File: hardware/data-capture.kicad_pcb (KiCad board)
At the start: 2 copper layers, 22 x 43.2 mm, 50 parts, among them J1 USB_B_Mini, J2 Conn_ARM_JTAG_SWD_10, J3 DM3AT-SF-PEJM5, J4 Conn_01x02, Q1 Q_PMOS_GSD, SW1 SW_Push, U1 MCP73831-2-OT, U2 TLV70218_SOT23-5, U3 AP2112K-3.3, U4 MDBT50Q-1M, U5 PCA9306, U6 ICM-20948, U7 BMP280, Y1 32.768

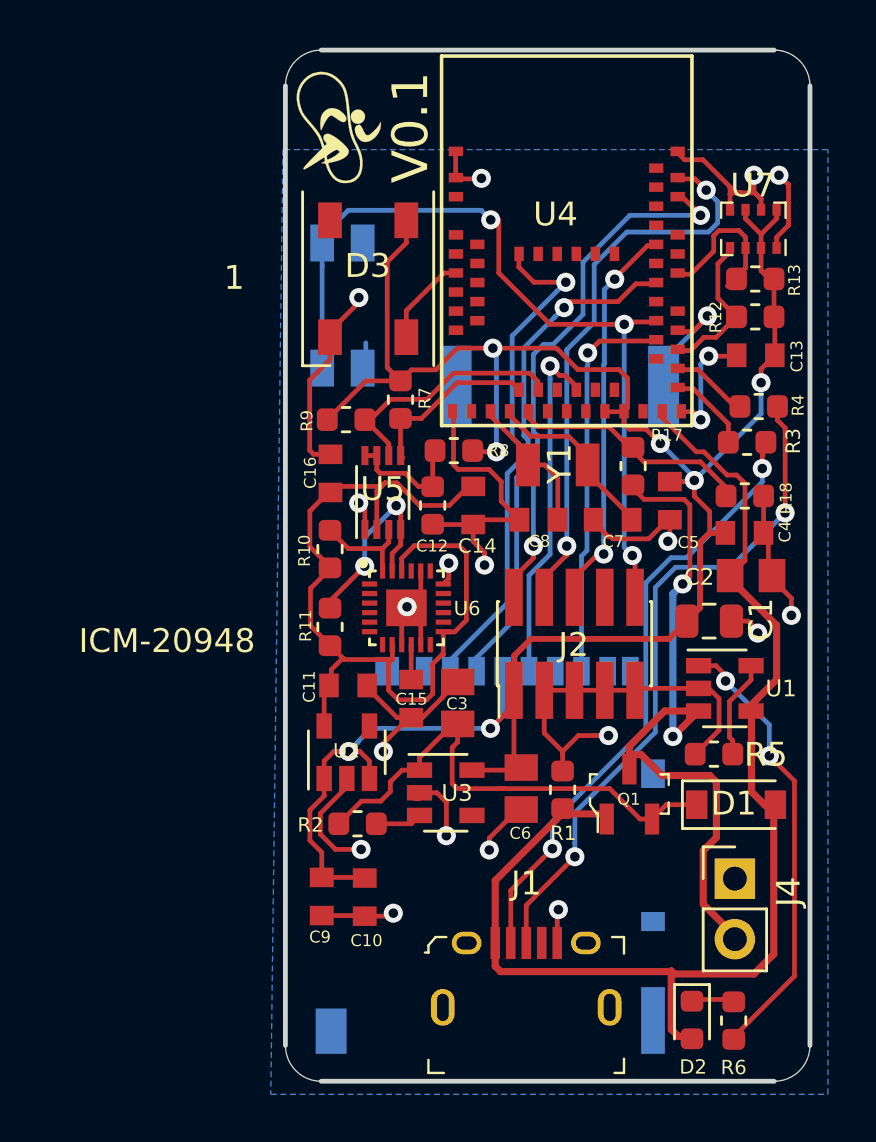
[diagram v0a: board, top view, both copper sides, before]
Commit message: update schematic for ESYNC for IMU
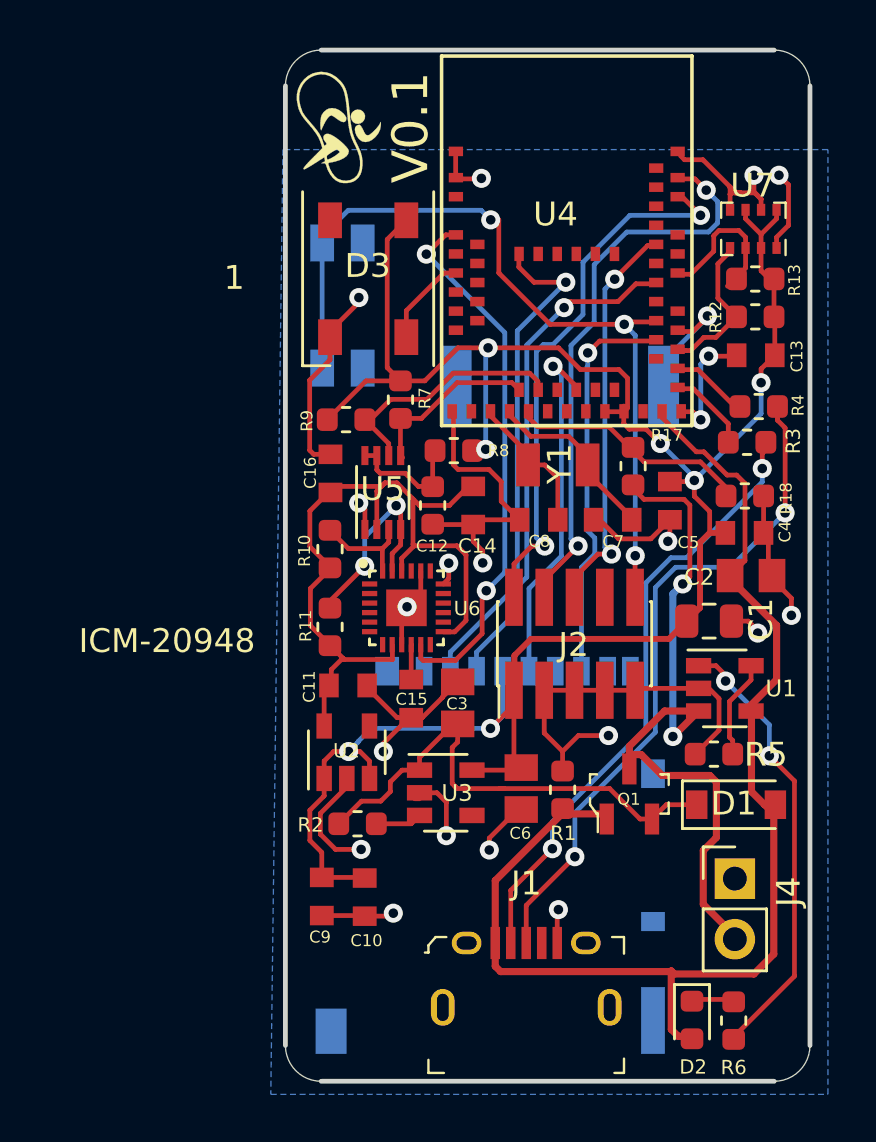
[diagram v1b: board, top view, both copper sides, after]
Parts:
- J2: value Conn_ARM_JTAG_SWD_10 -> Conn_ARM_JTAG_SWD_10-Connector_Specialized-bed-sensor-rescue-bed-sensor-rescue-bed-sensor-rescue-bed-sensor-rescue-bed-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
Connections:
- D3 pad 2: (no net) -> Net-(D3-Pad2)
- J1 pad 4: (no net) -> Net-(J1-Pad4)
- J2 pad 8: (no net) -> Net-(J2-Pad8)
- J3 pad 1: (no net) -> Net-(J3-Pad1)
- J3 pad 8: (no net) -> Net-(J3-Pad8)
- J3 pad SWA: (no net) -> Net-(J3-PadSWA)
- J3 pad SWB: (no net) -> Net-(J3-PadSWB)
- U2 pad 4: (no net) -> Net-(U2-Pad4)
- U3 pad 4: (no net) -> Net-(U3-Pad4)
- U4 pad 10: (no net) -> Net-(U4-Pad10)
- U4 pad 11: (no net) -> Net-(U4-Pad11)
- U4 pad 12: (no net) -> Net-(U4-Pad12)
- U4 pad 13: (no net) -> Net-(U4-Pad13)
- U4 pad 14: (no net) -> Net-(U4-Pad14)
- U4 pad 16: (no net) -> Net-(U4-Pad16)
- U4 pad 22: (no net) -> Net-(U4-Pad22)
- U4 pad 23: (no net) -> Net-(U4-Pad23)
- U4 pad 24: (no net) -> Net-(U4-Pad24)
- U4 pad 26: (no net) -> Net-(U4-Pad26)
- U4 pad 27: (no net) -> Net-(U4-Pad27)
- U4 pad 29: (no net) -> Net-(U4-Pad29)
- U4 pad 3: (no net) -> Net-(U4-Pad3)
- U4 pad 31: (no net) -> Net-(U4-Pad31)
- U4 pad 36: (no net) -> Net-(U4-Pad36)
- U4 pad 4: (no net) -> IMU_FSYC
- U4 pad 41: (no net) -> Net-(U4-Pad41)
- U4 pad 42: (no net) -> Net-(U4-Pad42)
- U4 pad 45: (no net) -> Net-(U4-Pad45)
- U4 pad 46: (no net) -> Net-(U4-Pad46)
- U4 pad 48: (no net) -> Net-(U4-Pad48)
- U4 pad 5: (no net) -> Net-(U4-Pad5)
- U4 pad 50: (no net) -> Net-(U4-Pad50)
- U4 pad 52: (no net) -> Net-(U4-Pad52)
- U4 pad 54: (no net) -> Net-(U4-Pad54)
- U4 pad 57: (no net) -> Net-(U4-Pad57)
- U4 pad 58: (no net) -> Net-(U4-Pad58)
- U4 pad 59: (no net) -> Net-(U4-Pad59)
- U4 pad 6: (no net) -> Net-(U4-Pad6)
- U4 pad 60: (no net) -> Net-(U4-Pad60)
- U4 pad 61: (no net) -> Net-(U4-Pad61)
- U4 pad 7: (no net) -> Net-(U4-Pad7)
- U4 pad 9: (no net) -> Net-(U4-Pad9)
- U6 pad 11: GND -> IMU_FSYC
- U6 pad 12: (no net) -> Net-(U6-Pad12)
- U6 pad 19: (no net) -> Net-(U6-Pad19)
- U6 pad 21: (no net) -> Net-(U6-Pad21)
- U6 pad 7: (no net) -> Net-(U6-Pad7)
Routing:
- net IMU_FSYC: track 0.00 -> 22.9 mm, vias 0 -> 2
- net +1V8: track 37.5 -> 33.1 mm
- net GND: track 98.7 -> 96.6 mm
